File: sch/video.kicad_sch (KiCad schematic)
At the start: 26 parts

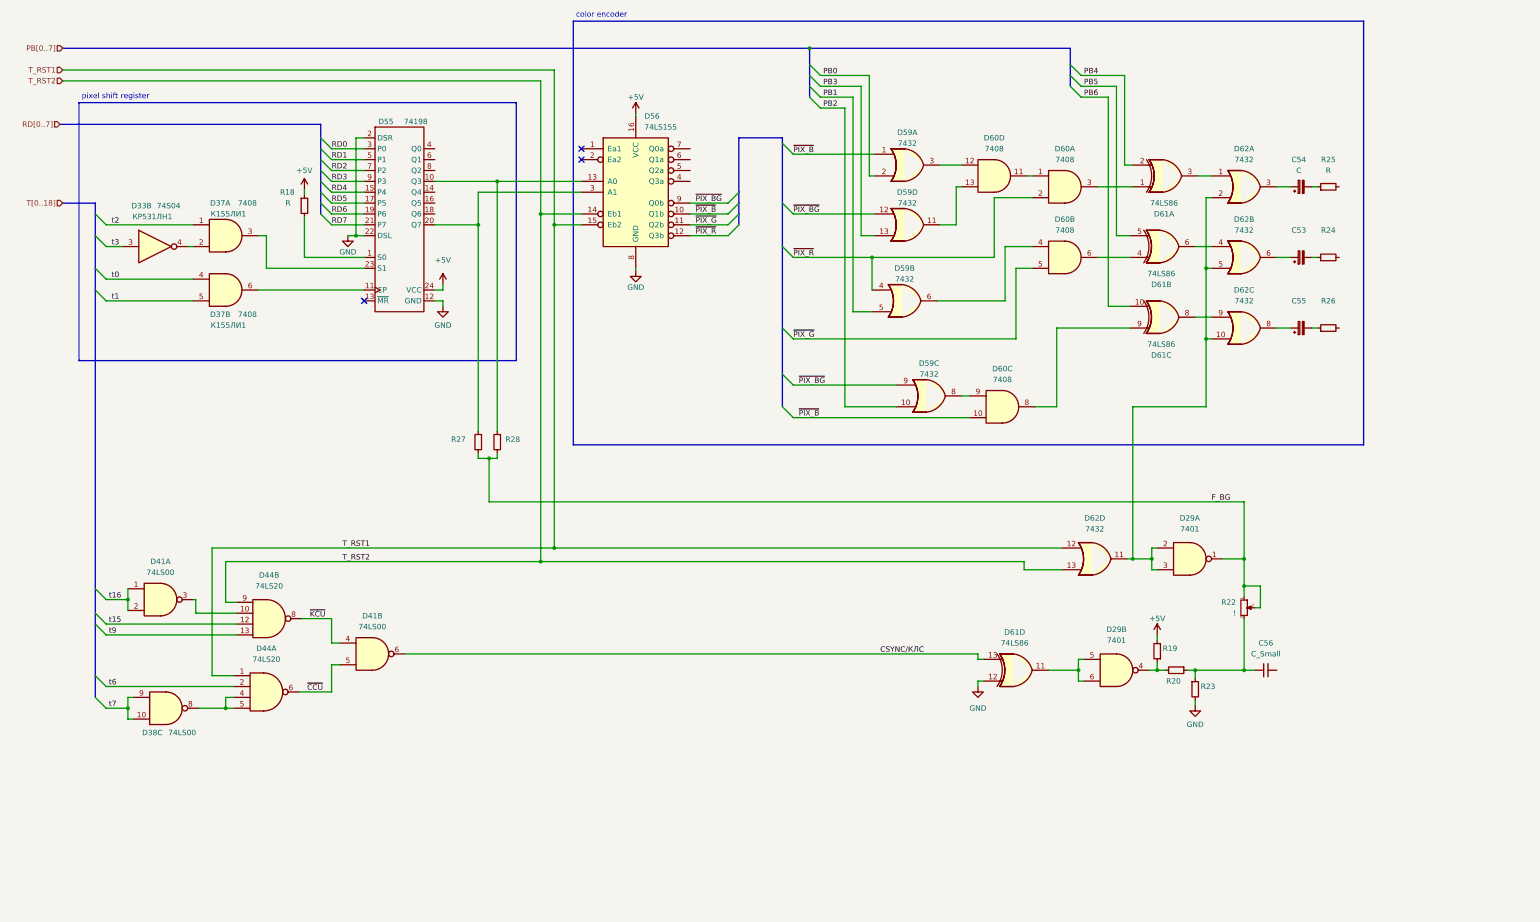
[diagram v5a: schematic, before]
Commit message: VSch: video block completed
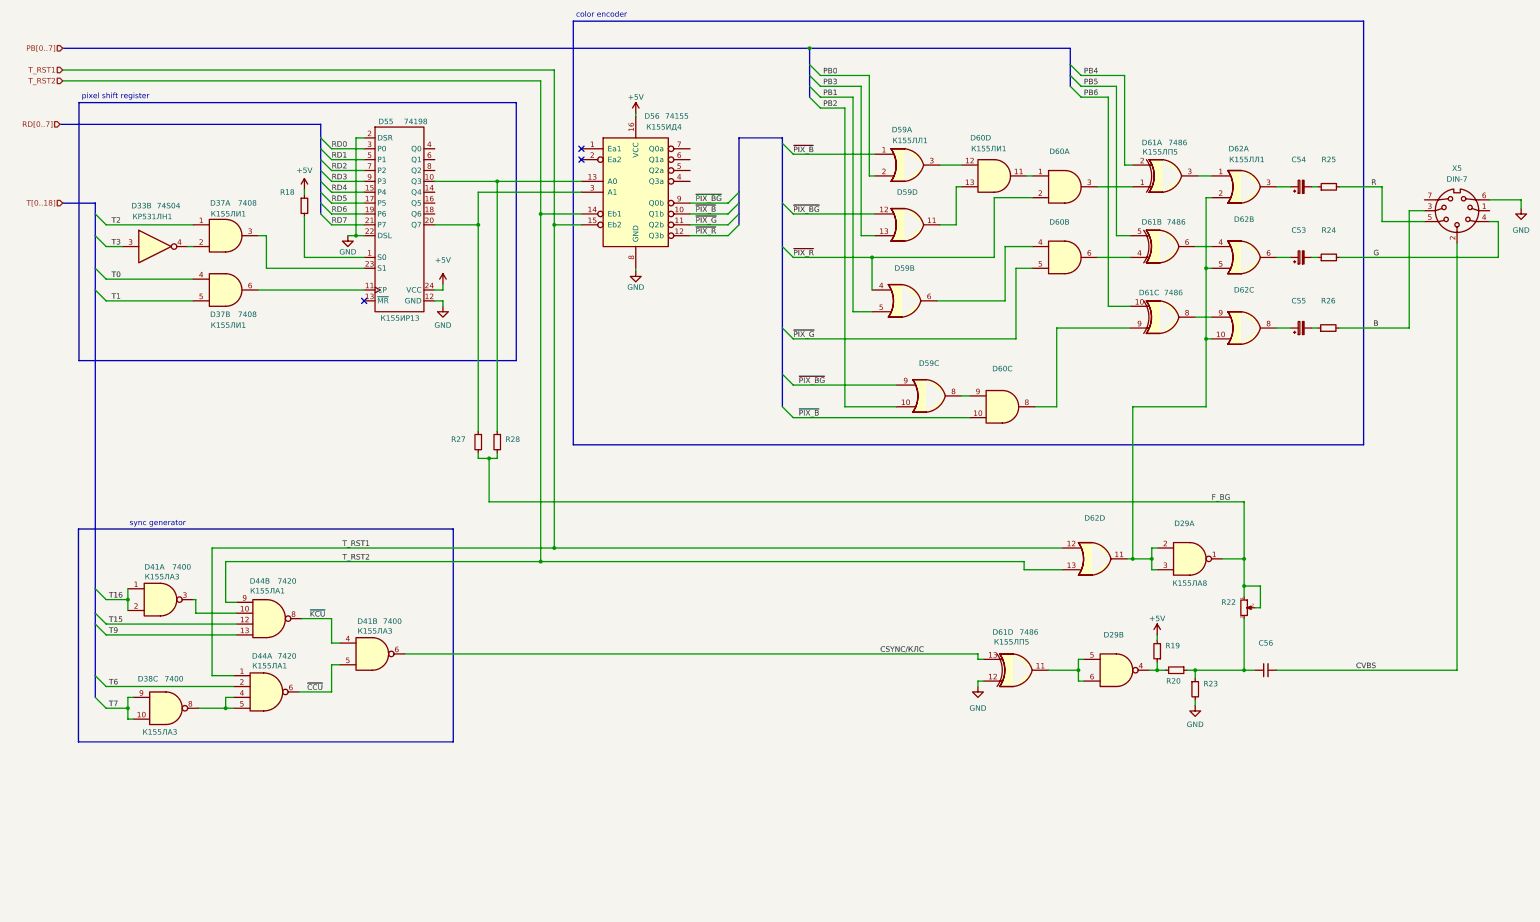
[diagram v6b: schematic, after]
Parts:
- added X5: DIN-7, symbol Connector:DIN-7
- C53, C55, R19, R20, R23, R24, R26, R27, R28: value ~ -> (none)
- C54: value C -> (none)
- C56: value C_Small -> (none)
- D29: value 7401 -> (none); CCCP (none) -> К155ЛА8
- D38, D41: value 74LS00 -> 7400; CCCP (none) -> К155ЛА3
- D44: value 74LS20 -> 7420; CCCP (none) -> К155ЛА1
- D55: CCCP (none) -> К155ИР13
- D56: value 74LS155 -> 74155; CCCP (none) -> К155ИД4
- D59, D62: value 7432 -> (none); CCCP (none) -> К155ЛЛ1
- D60: value 7408 -> (none); CCCP (none) -> К155ЛИ1
- D61: value 74LS86 -> 7486; CCCP (none) -> К155ЛП5
- R18, R25: value R -> (none)
- R22: value ! -> (none)
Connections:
- net GND: now also X5.6
- net R: now reaches R25.2
- net R: now also X5.5
- net B: now reaches R26.2
- net B: now also X5.3
- net CVBS: now reaches C56.2
- net CVBS: now also X5.2
- net G: now reaches R24.2
- net G: now also X5.4
- net t0 renamed T0
- net t1 renamed T1
- net t15 renamed T15
- net t16 renamed T16
- net t2 renamed T2
- net t3 renamed T3
- net t6 renamed T6
- net t7 renamed T7
- net t9 renamed T9
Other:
- note added: "sync generator"

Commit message: Schematics complete
Todo:
- part values
- full review
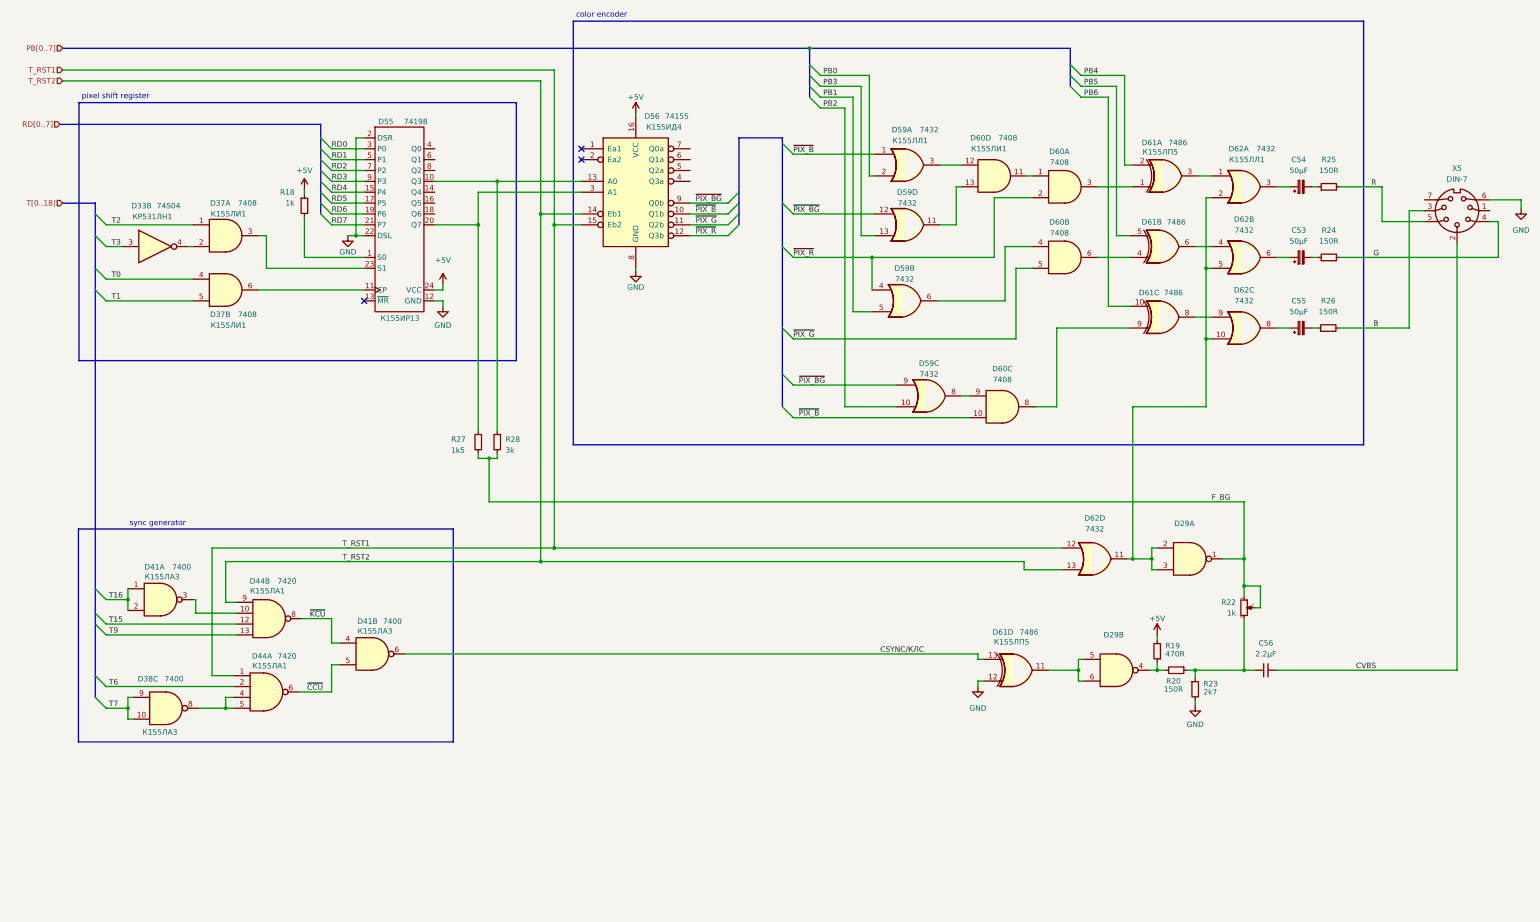
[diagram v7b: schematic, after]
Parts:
- C53, C54, C55: value (none) -> 50μF
- C56: value (none) -> 2.2μF
- D29: CCCP К155ЛА8 -> (none)
- D59, D62: value (none) -> 7432
- D60: value (none) -> 7408
- R18, R22: value (none) -> 1k
- R19: value (none) -> 470R
- R20, R24, R25, R26: value (none) -> 150R
- R23: value (none) -> 2k7
- R27: value (none) -> 1k5
- R28: value (none) -> 3k
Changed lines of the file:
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@@
     (in_bom yes) (on_board yes) (fields_autoplaced)
     (property "Reference" "D62" (id 0) (at 311.15 72.39 0))
-    (property "Value" "" (id 1) (at 311.15 74.93 0))
+    (property "Value" "7432" (id 1) (at 311.15 74.93 0))
     (property "Footprint" "" (id 2) (at 311.15 81.28 0)
       (effects (font (size 1.27 1.27)) hide)
@@
       (effects (font (size 1.27 1.27)) (justify right))
     )
-    (property "Value" "" (id 1) (at 138.43 126.365 0)
+    (property "Value" "3k" (id 1) (at 138.43 126.365 0)
       (effects (font (size 1.27 1.27)) (justify right))
     )
@@
     (in_bom yes) (on_board yes) (fields_autoplaced)
     (property "Reference" "R25" (id 0) (at 330.962 58.42 90))
-    (property "Value" "" (id 1) (at 330.962 60.96 90))
+    (property "Value" "150R" (id 1) (at 330.962 60.96 90))
     (property "Footprint" "" (id 2) (at 330.962 64.77 0)
       (effects (font (size 1.27 1.27)) hide)
@@
     (in_bom yes) (on_board yes)
     (property "Reference" "D59" (id 0) (at 232.41 66.04 0))
-    (property "Value" "" (id 1) (at 232.41 68.58 0))
+    (property "Value" "7432" (id 1) (at 232.41 68.58 0))
     (property "Footprint" "" (id 2) (at 232.41 73.66 0)
       (effects (font (size 1.27 1.27)) hide)
@@
       (effects (font (size 1.27 1.27)) (justify left))
     )
-    (property "Value" "" (id 1) (at 301.625 182.88 0)
+    (property "Value" "2k7" (id 1) (at 301.625 182.88 0)
       (effects (font (size 1.27 1.27)) (justify left))
     )
@@
     (in_bom yes) (on_board yes) (fields_autoplaced)
     (property "Reference" "R26" (id 0) (at 330.835 91.44 90))
-    (property "Value" "" (id 1) (at 330.835 93.98 90))
+    (property "Value" "150R" (id 1) (at 330.835 93.98 90))
     (property "Footprint" "" (id 2) (at 330.835 97.79 0)
       (effects (font (size 1.27 1.27)) hide)
@@
     (in_bom yes) (on_board yes)
     (property "Reference" "D60" (id 0) (at 249.555 53.34 0))
-    (property "Value" "" (id 1) (at 255.905 53.34 0))
+    (property "Value" "7408" (id 1) (at 255.905 53.34 0))
     (property "Footprint" "" (id 2) (at 252.73 62.23 0)
       (effects (font (size 1.27 1.27)) hide)
@@
     (in_bom yes) (on_board yes) (fields_autoplaced)
     (property "Reference" "C54" (id 0) (at 323.9389 58.42 90))
-    (property "Value" "" (id 1) (at 323.9389 60.96 90))
+    (property "Value" "50μF" (id 1) (at 323.9389 60.96 90))
     (property "Footprint" "" (id 2) (at 324.485 64.77 0)
       (effects (font (size 1.27 1.27)) hide)
@@
       (effects (font (size 1.27 1.27)) (justify right))
     )
-    (property "Value" "" (id 1) (at 309.245 164.4649 0)
+    (property "Value" "1k" (id 1) (at 309.245 164.4649 0)
       (effects (font (size 1.27 1.27)) (justify right))
     )
@@
     (in_bom yes) (on_board yes)
     (property "Reference" "R20" (id 0) (at 294.64 180.34 90))
-    (property "Value" "" (id 1) (at 294.64 182.245 90))
+    (property "Value" "150R" (id 1) (at 294.64 182.245 90))
     (property "Footprint" "" (id 2) (at 295.275 177.8 0)
       (effects (font (size 1.27 1.27)) hide)
@@
     (in_bom yes) (on_board yes)
     (property "Reference" "D62" (id 0) (at 309.88 55.88 0))
-    (property "Value" "" (id 1) (at 316.23 55.88 0))
+    (property "Value" "7432" (id 1) (at 316.23 55.88 0))
     (property "Footprint" "" (id 2) (at 311.15 64.77 0)
       (effects (font (size 1.27 1.27)) hide)
@@
     (in_bom yes) (on_board yes)
     (property "Reference" "D60" (id 0) (at 267.97 73.025 0))
-    (property "Value" "" (id 1) (at 267.97 75.565 0))
+    (property "Value" "7408" (id 1) (at 267.97 75.565 0))
     (property "Footprint" "" (id 2) (at 269.24 81.28 0)
       (effects (font (size 1.27 1.27)) hide)
@@
       (effects (font (size 1.27 1.27)) hide)
     )
-    (property "CCCP" "К155ЛА8" (id 4) (at 297.815 155.575 0)
-      (effects (font (size 1.27 1.27)) hide)
-    )
     (pin "1")
     (pin "2")
@@
       (effects (font (size 1.27 1.27)) hide)
     )
-    (property "CCCP" "К155ЛА8" (id 4) (at 298.45 157.48 0))
     (pin "1")
     (pin "2")
@@
     (in_bom yes) (on_board yes)
     (property "Reference" "D60" (id 0) (at 254.635 107.315 0))
-    (property "Value" "" (id 1) (at 254.635 109.855 0))
+    (property "Value" "7408" (id 1) (at 254.635 109.855 0))
     (property "Footprint" "" (id 2) (at 254.635 116.205 0)
       (effects (font (size 1.27 1.27)) hide)
@@
     (in_bom yes) (on_board yes) (fields_autoplaced)
     (property "Reference" "C56" (id 0) (at 316.2363 171.45 90))
-    (property "Value" "" (id 1) (at 316.2363 173.99 90))
+    (property "Value" "2.2μF" (id 1) (at 316.2363 173.99 90))
     (property "Footprint" "" (id 2) (at 316.23 177.8 0)
       (effects (font (size 1.27 1.27)) hide)
@@
     (in_bom yes) (on_board yes)
     (property "Reference" "D60" (id 0) (at 267.97 56.515 0))
-    (property "Value" "" (id 1) (at 267.97 59.055 0))
+    (property "Value" "7408" (id 1) (at 267.97 59.055 0))
     (property "Footprint" "" (id 2) (at 269.24 64.77 0)
       (effects (font (size 1.27 1.27)) hide)
@@
     (in_bom yes) (on_board yes)
     (property "Reference" "D59" (id 0) (at 237.49 106.045 0))
-    (property "Value" "" (id 1) (at 237.49 108.585 0))
+    (property "Value" "7432" (id 1) (at 237.49 108.585 0))
     (property "Footprint" "" (id 2) (at 237.49 113.665 0)
       (effects (font (size 1.27 1.27)) hide)
@@
       (effects (font (size 1.27 1.27)) (justify right))
     )
-    (property "Value" "" (id 1) (at 125.73 126.365 0)
+    (property "Value" "1k5" (id 1) (at 125.73 126.365 0)
       (effects (font (size 1.27 1.27)) (justify right))
     )
@@
     (in_bom yes) (on_board yes)
     (property "Reference" "D59" (id 0) (at 231.14 51.435 0))
-    (property "Value" "" (id 1) (at 237.49 51.435 0))
+    (property "Value" "7432" (id 1) (at 237.49 51.435 0))
     (property "Footprint" "" (id 2) (at 232.41 59.69 0)
       (effects (font (size 1.27 1.27)) hide)
@@
     (in_bom yes) (on_board yes) (fields_autoplaced)
     (property "Reference" "C53" (id 0) (at 323.9389 74.93 90))
-    (property "Value" "" (id 1) (at 323.9389 77.47 90))
+    (property "Value" "50μF" (id 1) (at 323.9389 77.47 90))
     (property "Footprint" "" (id 2) (at 324.485 81.28 0)
       (effects (font (size 1.27 1.27)) hide)
@@
       (effects (font (size 1.27 1.27)) (justify left))
     )
-    (property "Value" "" (id 1) (at 86.995 68.58 0)
+    (property "Value" "1k" (id 1) (at 86.995 68.58 0)
       (effects (font (size 1.27 1.27)) (justify left))
     )
@@
     (in_bom yes) (on_board yes) (fields_autoplaced)
     (property "Reference" "R24" (id 0) (at 330.962 74.93 90))
-    (property "Value" "" (id 1) (at 330.962 77.47 90))
+    (property "Value" "150R" (id 1) (at 330.962 77.47 90))
     (property "Footprint" "" (id 2) (at 330.962 81.28 0)
       (effects (font (size 1.27 1.27)) hide)
@@
       (effects (font (size 1.27 1.27)) (justify right))
     )
-    (property "Value" "" (id 1) (at 292.735 173.99 0)
+    (property "Value" "470R" (id 1) (at 292.735 173.99 0)
       (effects (font (size 1.27 1.27)) (justify right))
     )
@@
     (in_bom yes) (on_board yes) (fields_autoplaced)
     (property "Reference" "D62" (id 0) (at 311.15 88.9 0))
-    (property "Value" "" (id 1) (at 311.15 91.44 0))
+    (property "Value" "7432" (id 1) (at 311.15 91.44 0))
     (property "Footprint" "" (id 2) (at 311.15 97.79 0)
       (effects (font (size 1.27 1.27)) hide)
@@
     (in_bom yes) (on_board yes) (fields_autoplaced)
     (property "Reference" "D62" (id 0) (at 276.225 142.24 0))
-    (property "Value" "" (id 1) (at 276.225 144.78 0))
+    (property "Value" "7432" (id 1) (at 276.225 144.78 0))
     (property "Footprint" "" (id 2) (at 276.225 151.765 0)
       (effects (font (size 1.27 1.27)) hide)
@@
     (in_bom yes) (on_board yes) (fields_autoplaced)
     (property "Reference" "C55" (id 0) (at 323.9389 91.44 90))
-    (property "Value" "" (id 1) (at 323.9389 93.98 90))
+    (property "Value" "50μF" (id 1) (at 323.9389 93.98 90))
     (property "Footprint" "" (id 2) (at 324.485 97.79 0)
       (effects (font (size 1.27 1.27)) hide)
@@
     (in_bom yes) (on_board yes)
     (property "Reference" "D59" (id 0) (at 231.775 83.82 0))
-    (property "Value" "" (id 1) (at 231.775 86.36 0))
+    (property "Value" "7432" (id 1) (at 231.775 86.36 0))
     (property "Footprint" "" (id 2) (at 231.775 91.44 0)
       (effects (font (size 1.27 1.27)) hide)
